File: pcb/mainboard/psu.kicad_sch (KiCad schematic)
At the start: 127 parts, among them J1 CONN_PCIE_PWR_8PIN, J2 CONN_IBC_MGMT, J3 CONN_01X03, J4 CONN_01X05, SW1 SWITCH, SW2 SWITCH, U1 STM32L031C6U6, U2 MYMGK1R812ERSR, U26 LMR70503, U3 MYMGK00504ERSR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

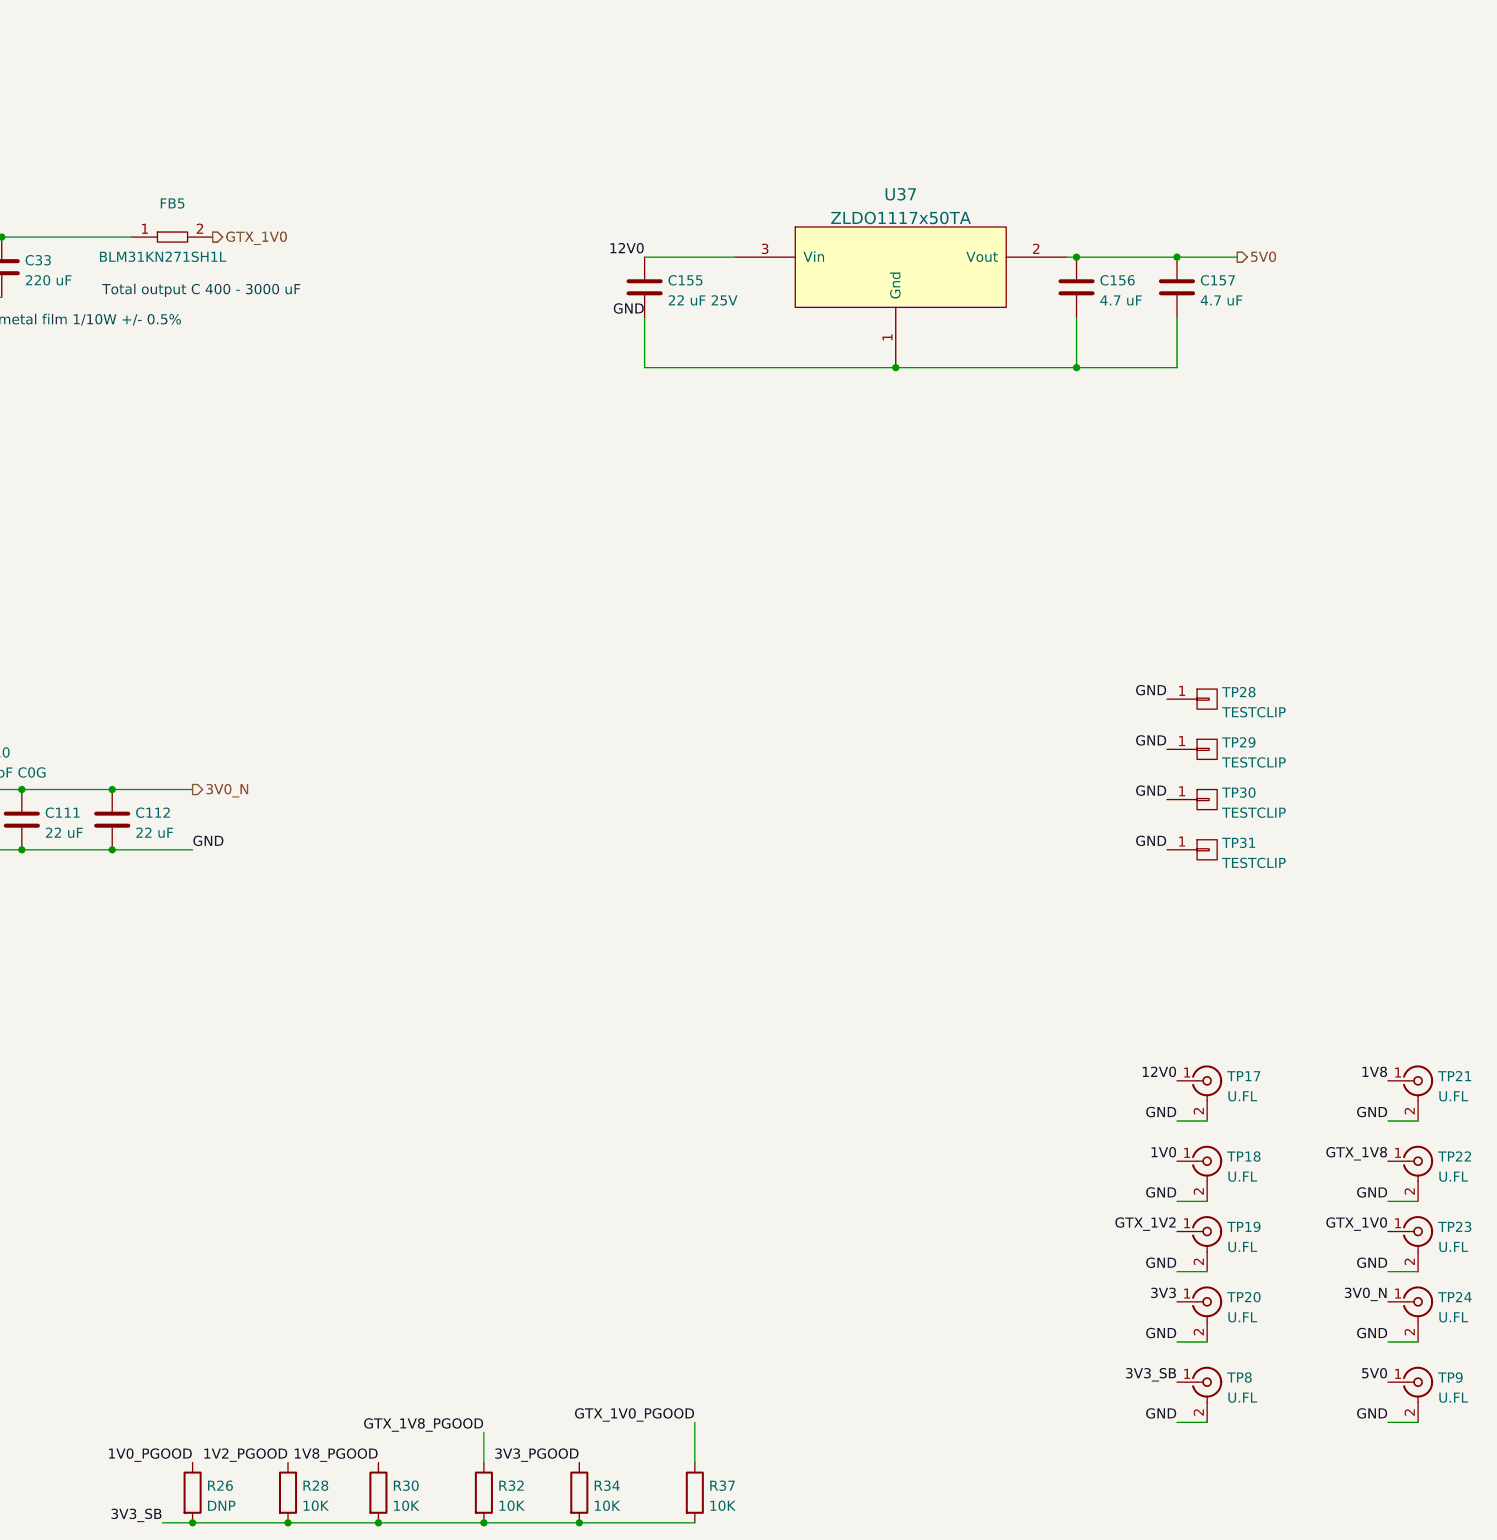
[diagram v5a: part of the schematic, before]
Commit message: Updated schematic with some notes on rework
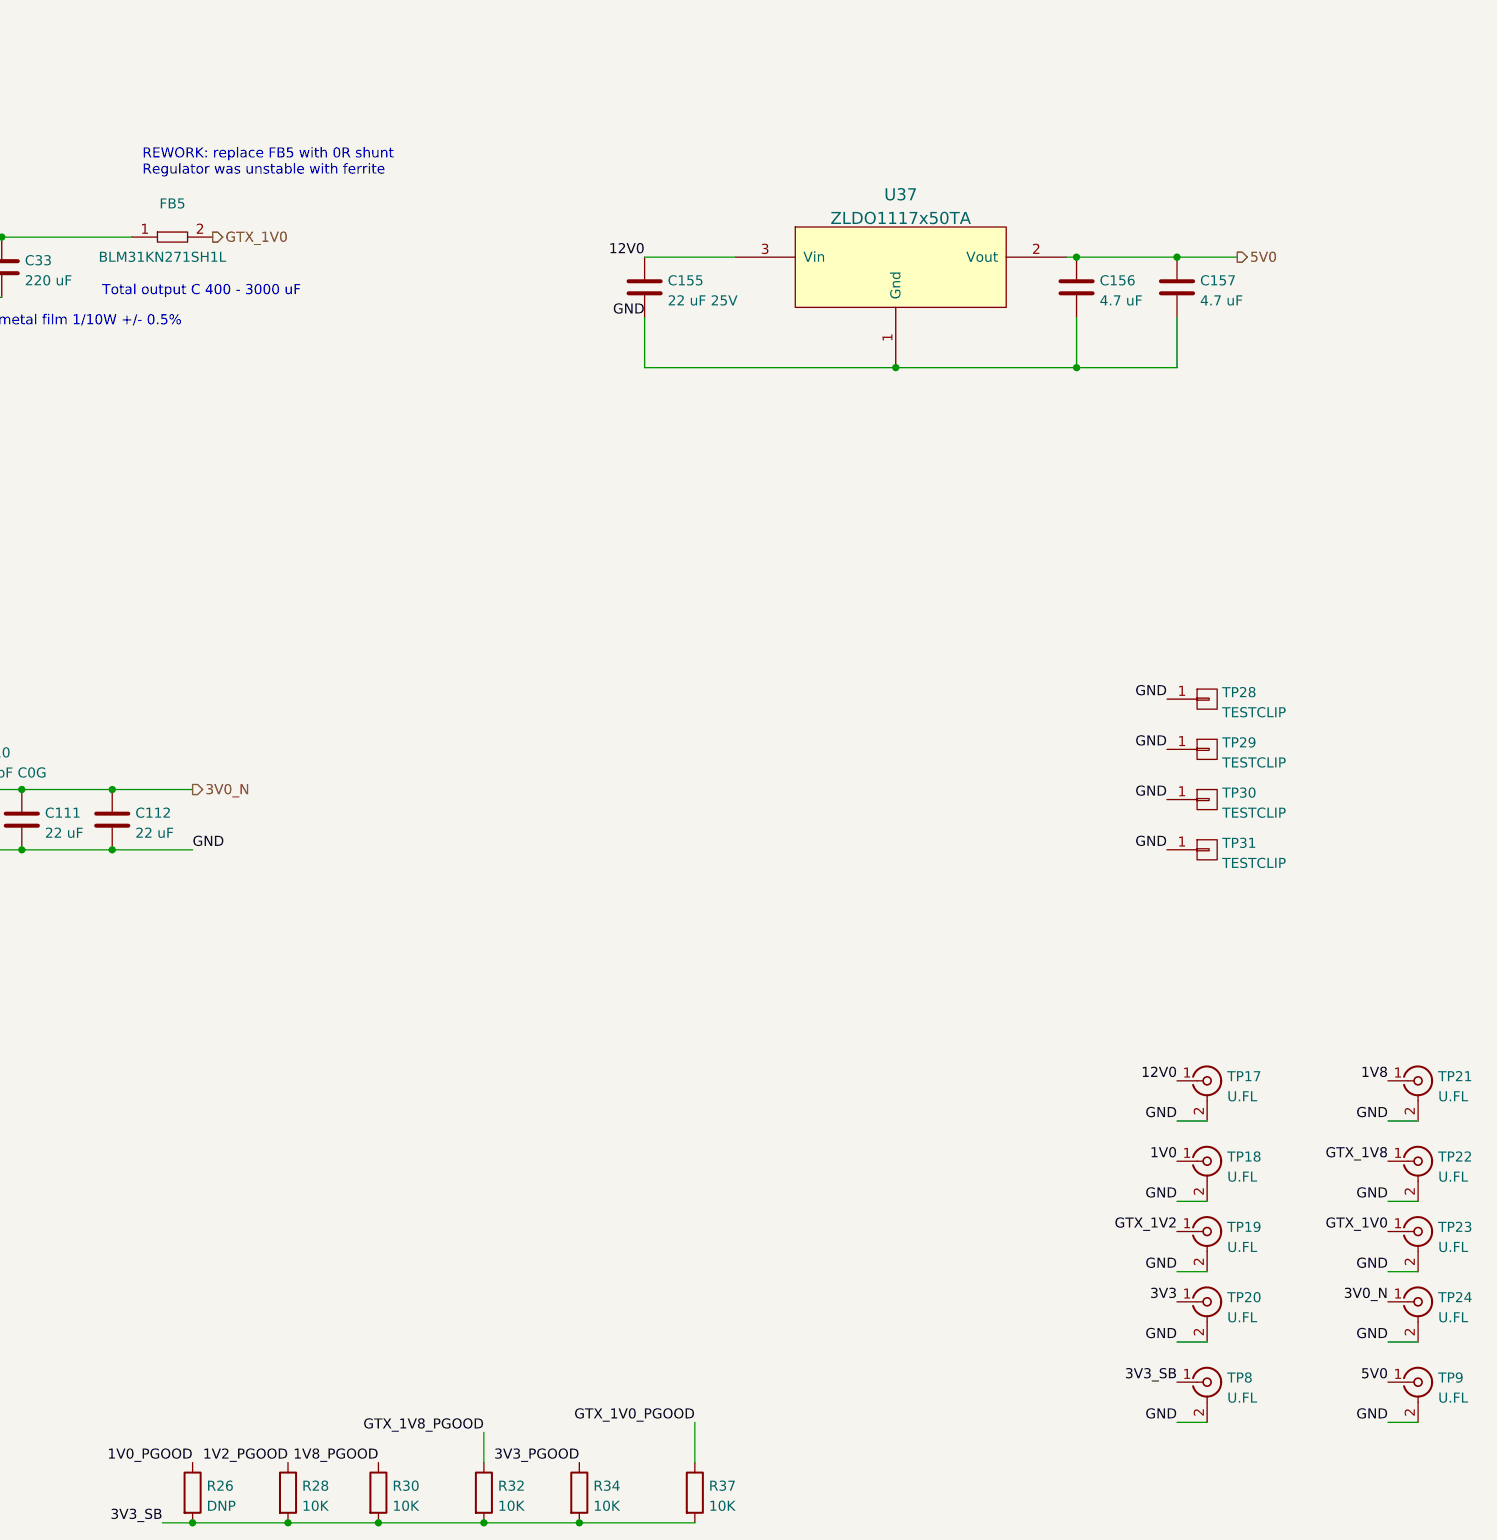
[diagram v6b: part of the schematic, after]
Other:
- note added: "REWORK: replace FB5 with 0R shunt Regulator was unstable with ferrite"
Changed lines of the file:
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@@
   (title_block
     (title "Trigger Crossbar")
-    (date "2023-12-26")
-    (rev "0.1")
+    (date "2024-02-25")
+    (rev "0.1-reworked")
     (company "Antikernel Labs")
     (comment 1 "Andrew D. Zonenberg")
@@
     (effects (font (size 1.27 1.27)) (justify left bottom))
   )
+  (text "REWORK: replace FB5 with 0R shunt\nRegulator was unstable with ferrite"
+    (at 318.77 189.23 0)
+    (effects (font (size 1.27 1.27)) (justify left bottom))
+  )
   (text "Total output C 400 - 3000 uF" (at 143.51 241.3 0)
     (effects (font (size 1.27 1.27)) (justify left bottom))
@@
       (effects (font (size 1.27 1.27)) hide)
     )
-    (pin "10")
-    (pin "11")
-    (pin "12")
-    (pin "13")
-    (pin "14" (alternate "SPI1_NSS"))
-    (pin "15" (alternate "SPI1_SCK"))
-    (pin "16" (alternate "SPI1_MISO"))
-    (pin "17")
-    (pin "29")
-    (pin "30" (alternate "I2C1_SCL"))
-    (pin "31" (alternate "I2C1_SDA"))
-    (pin "32")
-    (pin "33")
-    (pin "34")
-    (pin "37")
-    (pin "38")
-    (pin "18")
-    (pin "19" (alternate "ADC_IN9"))
-    (pin "20")
-    (pin "21")
-    (pin "22")
-    (pin "25")
-    (pin "26")
-    (pin "27")
-    (pin "28")
-    (pin "39")
-    (pin "40")
-    (pin "41")
-    (pin "42")
-    (pin "43")
-    (pin "45")
-    (pin "46")
-    (pin "1")
-    (pin "2")
-    (pin "3")
-    (pin "4")
     (pin "23")
     (pin "24")
@@
     (pin "9")
     (pin "PAD")
-    (pin "5")
-    (pin "6")
   )
   (symbol (lib_id "device:C") (at 217.17 370.84 0) (unit 1)
@@
       (effects (font (size 1.27 1.27)) hide)
     )
-    (pin "10")
-    (pin "11")
-    (pin "12")
-    (pin "13")
-    (pin "14" (alternate "SPI1_NSS"))
-    (pin "15" (alternate "SPI1_SCK"))
-    (pin "16" (alternate "SPI1_MISO"))
-    (pin "17")
-    (pin "29")
-    (pin "30" (alternate "I2C1_SCL"))
-    (pin "31" (alternate "I2C1_SDA"))
-    (pin "32")
-    (pin "33")
-    (pin "34")
-    (pin "37")
-    (pin "38")
     (pin "18")
     (pin "19" (alternate "ADC_IN9"))
@@
     (pin "45")
     (pin "46")
-    (pin "1")
-    (pin "2")
-    (pin "3")
-    (pin "4")
-    (pin "23")
-    (pin "24")
-    (pin "35")
-    (pin "36")
-    (pin "44")
-    (pin "47")
-    (pin "48")
-    (pin "7")
-    (pin "8")
-    (pin "9")
-    (pin "PAD")
-    (pin "5")
-    (pin "6")
   )
   (symbol (lib_id "conn:CONN_01X03") (at 281.94 387.35 0) (unit 1)
@@
     (pin "37")
     (pin "38")
-    (pin "18")
-    (pin "19" (alternate "ADC_IN9"))
-    (pin "20")
-    (pin "21")
-    (pin "22")
-    (pin "25")
-    (pin "26")
-    (pin "27")
-    (pin "28")
-    (pin "39")
-    (pin "40")
-    (pin "41")
-    (pin "42")
-    (pin "43")
-    (pin "45")
-    (pin "46")
-    (pin "1")
-    (pin "2")
-    (pin "3")
-    (pin "4")
-    (pin "23")
-    (pin "24")
-    (pin "35")
-    (pin "36")
-    (pin "44")
-    (pin "47")
-    (pin "48")
-    (pin "7")
-    (pin "8")
-    (pin "9")
-    (pin "PAD")
-    (pin "5")
-    (pin "6")
   )
   (symbol (lib_id "device:LED") (at 203.2 339.09 180) (unit 1)
@@
       (effects (font (size 1.27 1.27)) hide)
     )
-    (pin "10")
-    (pin "11")
-    (pin "12")
-    (pin "13")
-    (pin "14" (alternate "SPI1_NSS"))
-    (pin "15" (alternate "SPI1_SCK"))
-    (pin "16" (alternate "SPI1_MISO"))
-    (pin "17")
-    (pin "29")
-    (pin "30" (alternate "I2C1_SCL"))
-    (pin "31" (alternate "I2C1_SDA"))
-    (pin "32")
-    (pin "33")
-    (pin "34")
-    (pin "37")
-    (pin "38")
-    (pin "18")
-    (pin "19" (alternate "ADC_IN9"))
-    (pin "20")
-    (pin "21")
-    (pin "22")
-    (pin "25")
-    (pin "26")
-    (pin "27")
-    (pin "28")
-    (pin "39")
-    (pin "40")
-    (pin "41")
-    (pin "42")
-    (pin "43")
-    (pin "45")
-    (pin "46")
     (pin "1")
     (pin "2")
     (pin "3")
     (pin "4")
-    (pin "23")
-    (pin "24")
-    (pin "35")
-    (pin "36")
-    (pin "44")
-    (pin "47")
-    (pin "48")
-    (pin "7")
-    (pin "8")
-    (pin "9")
-    (pin "PAD")
-    (pin "5")
-    (pin "6")
   )
   (symbol (lib_id "device:C") (at 300.99 138.43 0) (unit 1)
@@
       (effects (font (size 1.27 1.27)) hide)
     )
-    (pin "10")
-    (pin "11")
-    (pin "12")
-    (pin "13")
-    (pin "14" (alternate "SPI1_NSS"))
-    (pin "15" (alternate "SPI1_SCK"))
-    (pin "16" (alternate "SPI1_MISO"))
-    (pin "17")
-    (pin "29")
-    (pin "30" (alternate "I2C1_SCL"))
-    (pin "31" (alternate "I2C1_SDA"))
-    (pin "32")
-    (pin "33")
-    (pin "34")
-    (pin "37")
-    (pin "38")
-    (pin "18")
-    (pin "19" (alternate "ADC_IN9"))
-    (pin "20")
-    (pin "21")
-    (pin "22")
-    (pin "25")
-    (pin "26")
-    (pin "27")
-    (pin "28")
-    (pin "39")
-    (pin "40")
-    (pin "41")
-    (pin "42")
-    (pin "43")
-    (pin "45")
-    (pin "46")
-    (pin "1")
-    (pin "2")
-    (pin "3")
-    (pin "4")
-    (pin "23")
-    (pin "24")
-    (pin "35")
-    (pin "36")
-    (pin "44")
-    (pin "47")
-    (pin "48")
-    (pin "7")
-    (pin "8")
-    (pin "9")
-    (pin "PAD")
     (pin "5")
     (pin "6")
